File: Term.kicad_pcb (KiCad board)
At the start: 2 copper layers, 21 parts, among them J1 JACK_TRS, P1 UART0, SW1 RESET, SW2 FLASH, SW3 SW_SPST, U1 LM1117-3.3, U2 ESP-12F

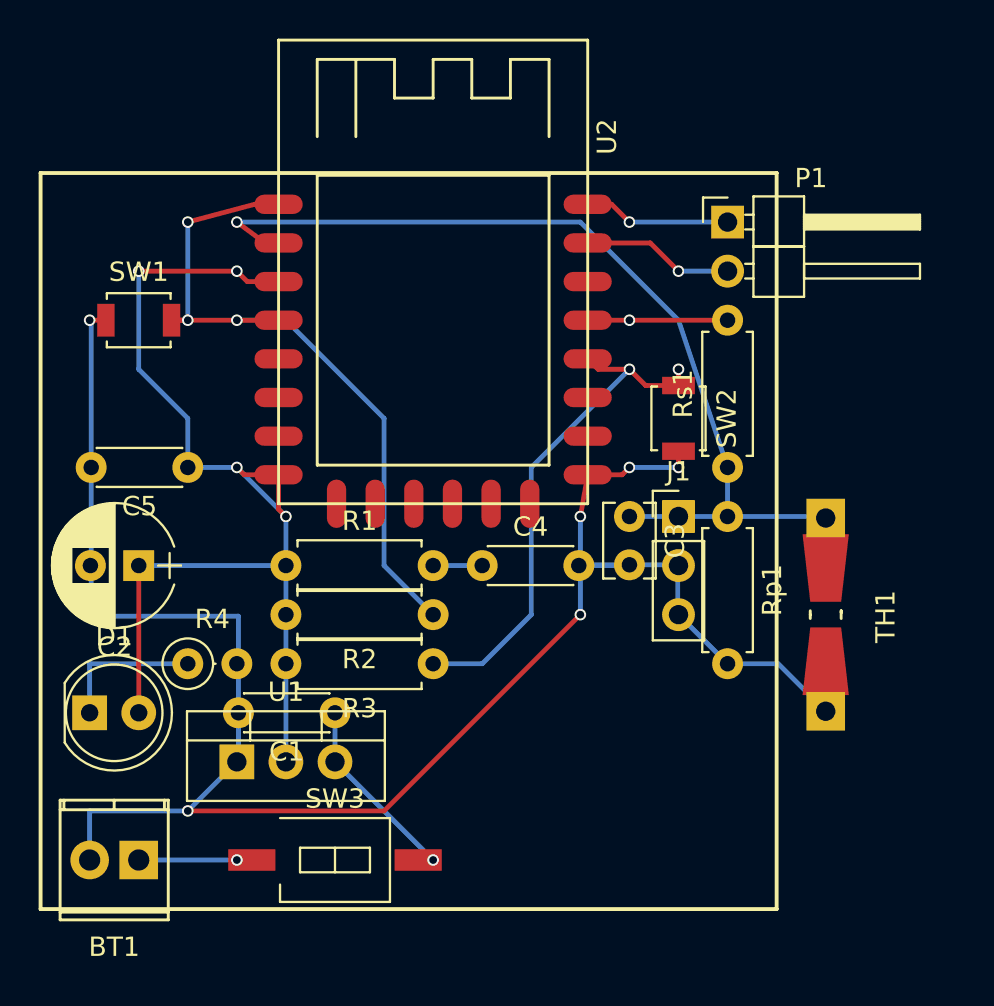
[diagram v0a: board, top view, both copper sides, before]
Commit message: v0.1 - Connection and deep sleep work.
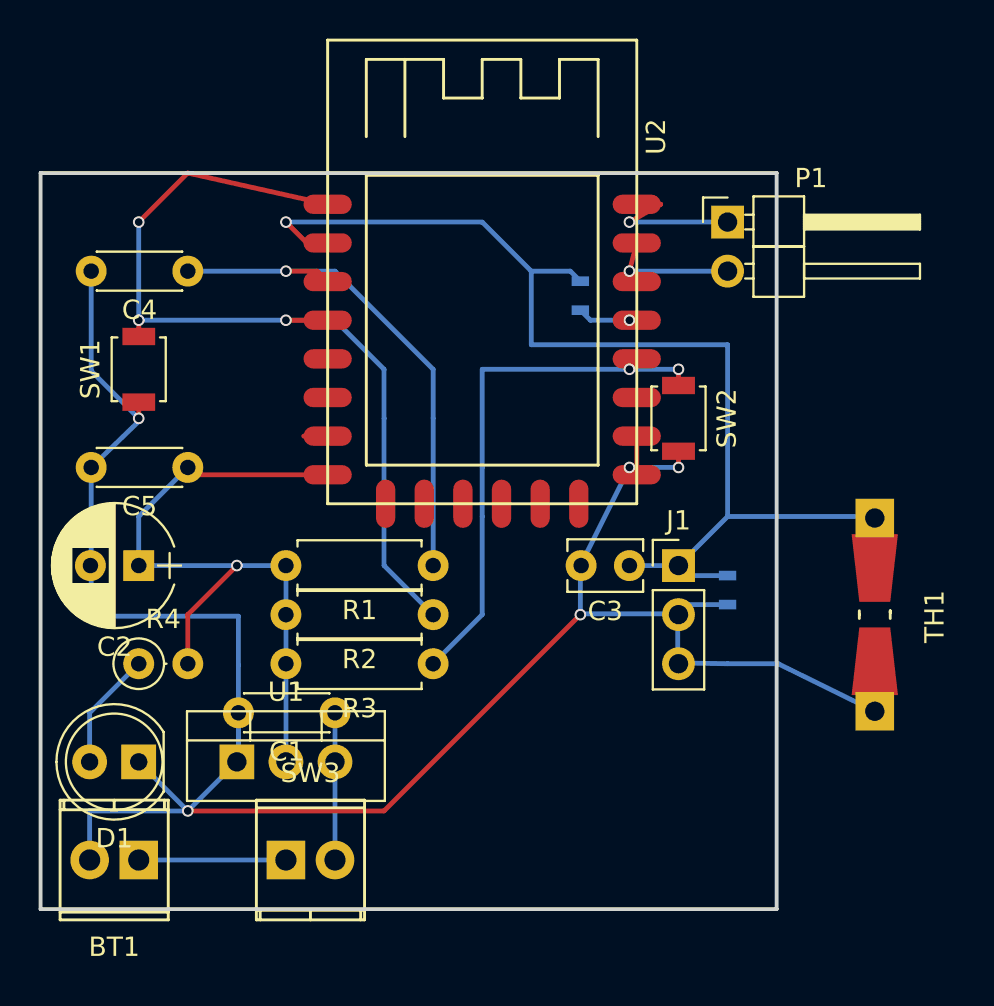
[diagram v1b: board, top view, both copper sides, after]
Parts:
- R1: value 10M -> 100k
- R2, R3: value 33k -> 22k
- R4: value 10k -> 2k2
- Rp1, Rs1: footprint Resistors_THT:R_Axial_DIN0207_L6.3mm_D2.5mm_P7.62mm_Horizontal -> Resistors_SMD:R_0603; moved to B.Cu
- SW3: footprint Buttons_Switches_SMD:SW_DIP_x1_W8.61mm_Slide_LowProfile -> Connectors_Terminal_Blocks:TerminalBlock_Pheonix_MPT-2.54mm_2pol
- moved C4 21.6 mm to (20.3, 17.8), turned to 180 degrees
- moved Rs1 11.7 mm to (40.6, 19.1), turned to 270 degrees
- moved R1 7.62 mm to (33.0, 33.0), turned to 180 degrees
- moved Rp1 3.81 mm to (48.3, 34.3)
- moved D1 3.59 mm to (17.8, 43.2), turned to 180 degrees
- moved C3 2.54 mm to (43.2, 33.0), turned to 180 degrees
- moved J1 2.54 mm to (45.7, 33.0)
- moved SW3 2.54 mm to (25.4, 48.3)
- moved R4 2.54 mm to (17.8, 38.1)
- moved SW1 2.54 mm to (17.8, 22.9), turned to 90 degrees
- moved TH1 2.54 mm to (55.9, 35.6)
- moved U2 2.54 mm to (35.6, 20.3)
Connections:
- D1 pad 1: Net-(D1-Pad1) -> GND
- D1 pad 2: +3V3 -> Net-(D1-Pad2)
- R1 pad 1: +3V3 -> Net-(C4-Pad1)
- R1 pad 2: Net-(C4-Pad1) -> +3V3
- R4 pad 1: Net-(D1-Pad1) -> Net-(D1-Pad2)
- R4 pad 2: GND -> +3V3
- U2 pad 16: Net-(U2-Pad16) -> GND
- U2 pad 3: +3V3 -> Net-(C4-Pad1)
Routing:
- net Net-(C4-Pad1): track 2.54 -> 28.3 mm, vias 0 -> 2
- net +3V3: track 57.4 -> 37.4 mm, vias 4 -> 1
- net GND: track 105.3 -> 116.7 mm, vias 6 -> 5
- net /ADC: track 50.8 -> 61.1 mm
- net /~RST: track 37.2 -> 46.6 mm
- net Net-(D1-Pad1): track 7.62 -> 0.00 mm
- net Net-(D1-Pad2): track 0.00 -> 6.13 mm
- net /SENSE_PWR: track 7.24 -> 4.03 mm
- net Net-(C1-Pad1): track 10.5 -> 7.62 mm
- net Net-(R3-Pad1): track 27.0 -> 29.0 mm
- net Net-(U2-Pad7): track 0.00 -> 1.24 mm
- net Net-(P1-Pad1): track 7.62 -> 8.18 mm
- net Net-(BT1-Pad1): track 8.18 -> 7.62 mm, vias 1 -> 0
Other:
- board outline added: 38.1 x 38.1 mm
